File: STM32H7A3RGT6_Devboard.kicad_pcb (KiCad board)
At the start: 2 copper layers, 1 part, among them U1 STM32H7A3RGT6

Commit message: First full draft
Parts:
- added C1: 2u2, Capacitor_SMD:C_0402_1005Metric_Pad0.74x0.62mm_HandSolder, F.Cu at (121.0, 97.2)
- added C10: 1u, Capacitor_SMD:C_0402_1005Metric_Pad0.74x0.62mm_HandSolder, B.Cu at (136.1, 104.5)
- added C11: 1uF, Capacitor_SMD:C_0402_1005Metric_Pad0.74x0.62mm_HandSolder, F.Cu at (106.8, 95.0)
- added C12: 1uF, Capacitor_SMD:C_0402_1005Metric_Pad0.74x0.62mm_HandSolder, F.Cu at (110.7, 96.4)
- added C13: 8pF, Capacitor_SMD:C_0402_1005Metric_Pad0.74x0.62mm_HandSolder, F.Cu at (136.3, 107.5)
- added C14: 8pF, Capacitor_SMD:C_0402_1005Metric_Pad0.74x0.62mm_HandSolder, F.Cu at (140.4, 107.6)
- added C15: 1uF, Capacitor_SMD:C_0603_1608Metric_Pad1.08x0.95mm_HandSolder, F.Cu at (149.3, 100.0)
- added C2: 1u, Capacitor_SMD:C_0402_1005Metric_Pad0.74x0.62mm_HandSolder, F.Cu at (140.3, 95.6)
- added C3: 100n, Capacitor_SMD:C_0402_1005Metric_Pad0.74x0.62mm_HandSolder, F.Cu at (131.2, 107.8)
- added C4: 100n, Capacitor_SMD:C_0402_1005Metric_Pad0.74x0.62mm_HandSolder, F.Cu at (122.2, 98.8)
- added C5: 100n, Capacitor_SMD:C_0402_1005Metric_Pad0.74x0.62mm_HandSolder, F.Cu at (131.2, 92.2)
- added C6: 100n, Capacitor_SMD:C_0402_1005Metric_Pad0.74x0.62mm_HandSolder, F.Cu at (137.5, 97.2)
- added C7: 100n, Capacitor_SMD:C_0402_1005Metric_Pad0.74x0.62mm_HandSolder, F.Cu at (128.8, 107.8)
- added C8: 4u7, Capacitor_SMD:C_0603_1608Metric, F.Cu at (117.8, 97.9)
- added C9: 100n, Capacitor_SMD:C_0402_1005Metric_Pad0.74x0.62mm_HandSolder, F.Cu at (137.8, 103.2)
- added D1: DF2B7AE, Diode_SMD:D_SOD-523, F.Cu at (104.7, 96.9)
- added D2: LED, LED_SMD:LED_0603_1608Metric, F.Cu at (106.9, 107.5)
- added D3: LED, LED_SMD:LED_0603_1608Metric, F.Cu at (103.5, 92.9)
- added J1: USB_C_Receptacle_USB2.0_14P, USBC:USB_C_Receptacle_Molex_217179-0001, F.Cu at (100.0, 100.0)
- added J2: Conn_01x04_Socket, Connector_PinHeader_2.54mm:PinHeader_1x04_P2.54mm_Vertical, F.Cu at (112.0, 100.4)
- added J3: Conn_01x25_PinHeader, Connector_PinHeader_2.54mm:PinHeader_1x25_P2.54mm_Vertical, B.Cu at (98.3, 88.6)
- added J4: Conn_01x25_PinHeader, Connector_PinHeader_2.54mm:PinHeader_1x25_P2.54mm_Vertical, B.Cu at (98.3, 111.4)
- added R1: 5k1, Resistor_SMD:R_0603_1608Metric, F.Cu at (99.9, 93.2)
- added R2: 5k1, Resistor_SMD:R_0603_1608Metric, F.Cu at (99.9, 106.8)
- added R3: 1k, Resistor_SMD:R_0603_1608Metric_Pad0.98x0.95mm_HandSolder, F.Cu at (109.3, 106.8)
- added R4: 5k1, Resistor_SMD:R_0603_1608Metric, F.Cu at (146.8, 99.2)
- added R5: 5k1, Resistor_SMD:R_0603_1608Metric, F.Cu at (103.4, 106.8)
- added R6: 1k, Resistor_SMD:R_0603_1608Metric_Pad0.98x0.95mm_HandSolder, F.Cu at (106.0, 92.1)
- added SW1: RESET, Button_Switch_SMD:SW_Push_1P1T-SH_NO_CK_KMR2xxG, F.Cu at (143.2, 99.2)
- added SW2: BOOT, Button_Switch_SMD:SW_Push_1P1T-SH_NO_CK_KMR2xxG, F.Cu at (106.8, 104.2)
- added U2: AP2127N-3.3TRG1, Package_TO_SOT_SMD:SOT-23, F.Cu at (108.2, 96.8)
- added U3: USBLC6-2SC6, Package_TO_SOT_SMD:SOT-23-6, F.Cu at (106.3, 100.0)
- added Y1: 12MHz, Crystal:Crystal_SMD_2016-4Pin_2.0x1.6mm, F.Cu at (138.4, 107.5)
- moved U1 10.8 mm to (130.0, 100.0), turned to 135 degrees
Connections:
- U1 pad 10: unconnected-(U1-PC2-Pad10) -> /PC2
- U1 pad 11: unconnected-(U1-PC3-Pad11) -> /PC3
- U1 pad 14: unconnected-(U1-PA0-Pad14) -> /PA0
- U1 pad 15: unconnected-(U1-PA1-Pad15) -> /PA1
- U1 pad 16: unconnected-(U1-PA2-Pad16) -> /PA2
- U1 pad 17: unconnected-(U1-PA3-Pad17) -> /PA3
- U1 pad 2: unconnected-(U1-PC13-Pad2) -> /PC13
- U1 pad 20: unconnected-(U1-PA4-Pad20) -> /PA4
- U1 pad 21: unconnected-(U1-PA5-Pad21) -> /PA5
- U1 pad 22: unconnected-(U1-PA6-Pad22) -> /PA6
- U1 pad 23: unconnected-(U1-PA7-Pad23) -> /PA7
- U1 pad 24: unconnected-(U1-PC4-Pad24) -> /PC4
- U1 pad 25: unconnected-(U1-PC5-Pad25) -> /PC5
- U1 pad 26: unconnected-(U1-PB0-Pad26) -> /PB0
- U1 pad 27: unconnected-(U1-PB1-Pad27) -> /PB1
- U1 pad 28: unconnected-(U1-PB2-Pad28) -> /PB2
- U1 pad 29: unconnected-(U1-PB10-Pad29) -> /PB10
- U1 pad 3: unconnected-(U1-PC14-Pad3) -> /PC14
- U1 pad 33: unconnected-(U1-PB12-Pad33) -> /PB12
- U1 pad 34: unconnected-(U1-PB13-Pad34) -> /PB13
- U1 pad 35: unconnected-(U1-PB14-Pad35) -> /PB14
- U1 pad 36: unconnected-(U1-PB15-Pad36) -> /PB15
- U1 pad 37: unconnected-(U1-PC6-Pad37) -> /PC6
- U1 pad 38: unconnected-(U1-PC7-Pad38) -> /PC7
- U1 pad 39: unconnected-(U1-PC9-Pad39) -> /PC9
- U1 pad 4: unconnected-(U1-PC15-Pad4) -> /PC15
- U1 pad 40: unconnected-(U1-PA8-Pad40) -> /PA8
- U1 pad 41: unconnected-(U1-PA9-Pad41) -> /PA9
- U1 pad 42: unconnected-(U1-PA10-Pad42) -> /PA10
- U1 pad 43: unconnected-(U1-PA11-Pad43) -> /USB_D-
- U1 pad 44: unconnected-(U1-PA12-Pad44) -> /USB_D+
- U1 pad 45: unconnected-(U1-PA13-Pad45) -> /SWDIO
- U1 pad 49: unconnected-(U1-PA14-Pad49) -> /SWCLK
- U1 pad 5: unconnected-(U1-PH0-Pad5) -> /OSC_IN
- U1 pad 50: unconnected-(U1-PA15-Pad50) -> /PA15
- U1 pad 51: unconnected-(U1-PC10-Pad51) -> /PC10
- U1 pad 52: unconnected-(U1-PC11-Pad52) -> /PC11
- U1 pad 53: unconnected-(U1-PC12-Pad53) -> /PC12
- U1 pad 54: unconnected-(U1-PD2-Pad54) -> /PD2
- U1 pad 55: unconnected-(U1-PB3-Pad55) -> /PB3
- U1 pad 56: unconnected-(U1-PB4-Pad56) -> /PB4
- U1 pad 57: unconnected-(U1-PB5-Pad57) -> /PB5
- U1 pad 58: unconnected-(U1-PB6-Pad58) -> /PB6
- U1 pad 59: unconnected-(U1-PB7-Pad59) -> /PB7
- U1 pad 6: unconnected-(U1-PH1-Pad6) -> /OSC_OUT
- U1 pad 61: unconnected-(U1-PB8-Pad61) -> /PB8
- U1 pad 62: unconnected-(U1-PB9-Pad62) -> /PB9
- U1 pad 8: unconnected-(U1-PC0-Pad8) -> /PC0
- U1 pad 9: unconnected-(U1-PC1-Pad9) -> /PC1
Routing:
- net +3V3: track 0.00 -> 172.0 mm, vias 0 -> 9
- net VBUS: track 0.00 -> 36.8 mm
- net /BOOT0: track 0.00 -> 25.5 mm, vias 0 -> 2
- net /PA3: track 0.00 -> 24.9 mm
- net /PA4: track 0.00 -> 24.9 mm, vias 0 -> 2
- net /PA2: track 0.00 -> 24.3 mm
- net /PA0: track 0.00 -> 23.0 mm, vias 0 -> 2
- net /PA10: track 0.00 -> 22.8 mm
- net /PC2: track 0.00 -> 22.3 mm, vias 0 -> 2
- net /PA1: track 0.00 -> 22.1 mm
- net /PA15: track 0.00 -> 21.8 mm
- net /PA9: track 0.00 -> 20.5 mm
- net /NRST: track 0.00 -> 20.4 mm, vias 0 -> 2
- net /PA5: track 0.00 -> 20.0 mm
- net /USB_D-: track 0.00 -> 19.8 mm
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- added copper zone on B.Cu, net GND
- added copper zone on F.Cu, net GND
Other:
- board outline added: 63.7 x 25.7 mm

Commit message: update
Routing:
- net GND: track 15.8 -> 22.1 mm, vias 42 -> 59
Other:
- board size 63.7 x 25.7 mm -> 63.8 x 25.7 mm

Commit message: appease DRC checker
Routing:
- net +3V3: track 172.0 -> 170.6 mm
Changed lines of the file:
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@@
 		(tags "Diode SOD523")
 		(property "Reference" "D1"
-			(at 1.9 0 0)
+			(at 1.8 0 0)
 			(layer "F.SilkS")
 			(effects
@@
 		(tags "capacitor handsolder")
 		(property "Reference" "C9"
-			(at -0.022981 -1.154352 0)
+			(at 0.0325 1.25 0)
 			(layer "F.SilkS")
 			(effects
@@
 		(tags "SOT TO_SOT_SMD")
 		(property "Reference" "U2"
-			(at 0 2.25 180)
+			(at 0 2.15 180)
 			(layer "F.SilkS")
 			(effects
@@
 		(tags "capacitor handsolder")
 		(property "Reference" "C11"
-			(at 1.7325 0 0)
+			(at 1.6325 0 0)
 			(layer "F.SilkS")
 			(effects
@@
 		)
 		(property "Value" "BOOT"
-			(at 0 0 0)
+			(at -4.7 0 0)
 			(layer "F.SilkS")
 			(effects
@@
 	)
 	(via
-		(at 110.1 103.9)
+		(at 110.1 103.2)
 		(size 0.7)
 		(drill 0.4)
@@
 		(width 0.5)
 		(layer "B.Cu")
-		(net "+3V3")
-	)
-	(segment
-		(start 137.931371 95.1)
-		(end 138.9 96.068629)
-		(width 0.5)
-		(layer "B.Cu")

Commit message: Fix more DRC check errors
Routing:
- net VBUS: track 36.8 -> 38.2 mm
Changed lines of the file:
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@@
 		(capping no)
 		(filling no)
-		(zone_defaults)
 		(pcbplotparams
 			(layerselection 0x00000000_00000000_55555555_5755f5ff)
@@
 	)
 	(segment
+		(start 106.8 95.6)
+		(end 106.8 96.2375)
+		(width 0.5)
+		(layer "F.Cu")
+		(net "VBUS")
+	)
+	(segment
 		(start 105.3 97.6)
 		(end 106.325 98.625)
@@
 		(width 0.5)
 		(layer "F.Cu")
+		(net "VBUS")
+	)
+	(segment
+		(start 106.8 96.2375)
+		(end 107.3125 96.75)
+		(width 0.5)
+		(layer "F.Cu")

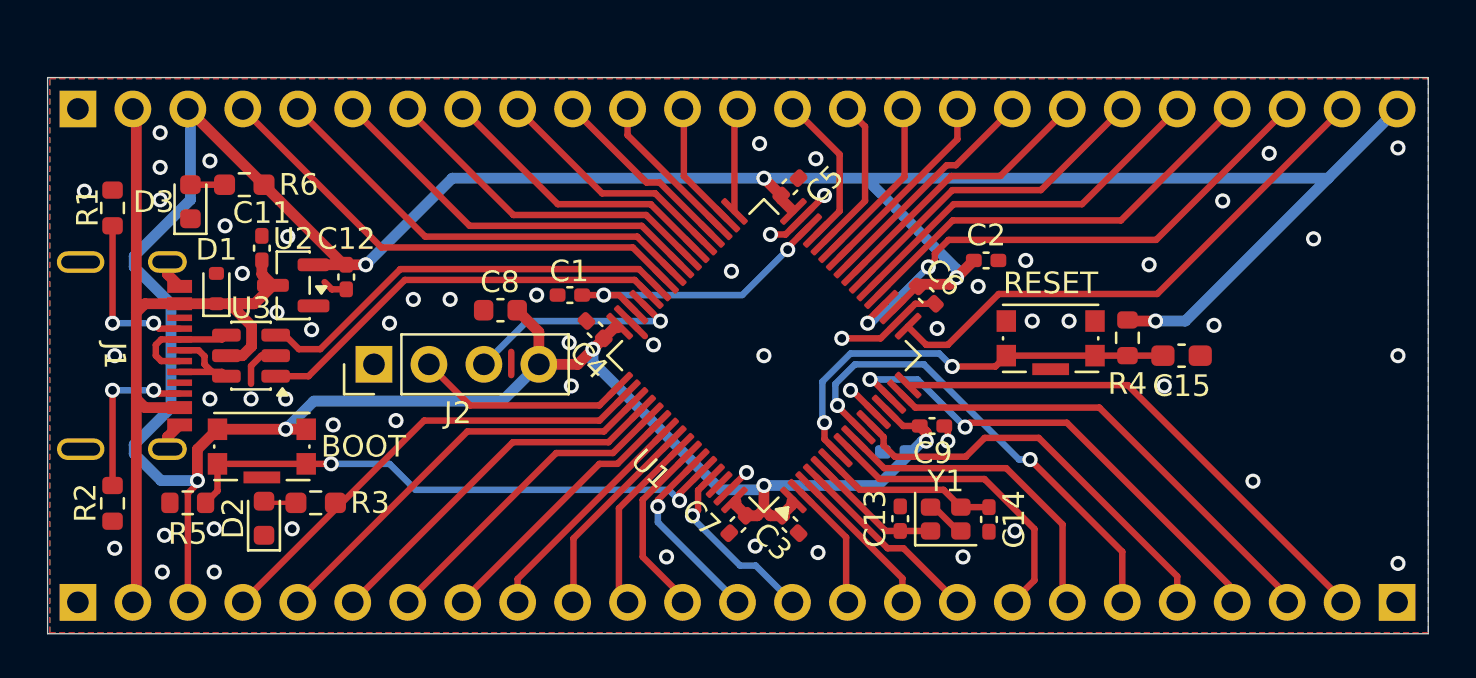
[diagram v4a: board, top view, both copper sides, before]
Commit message: Silkscreen and more vias
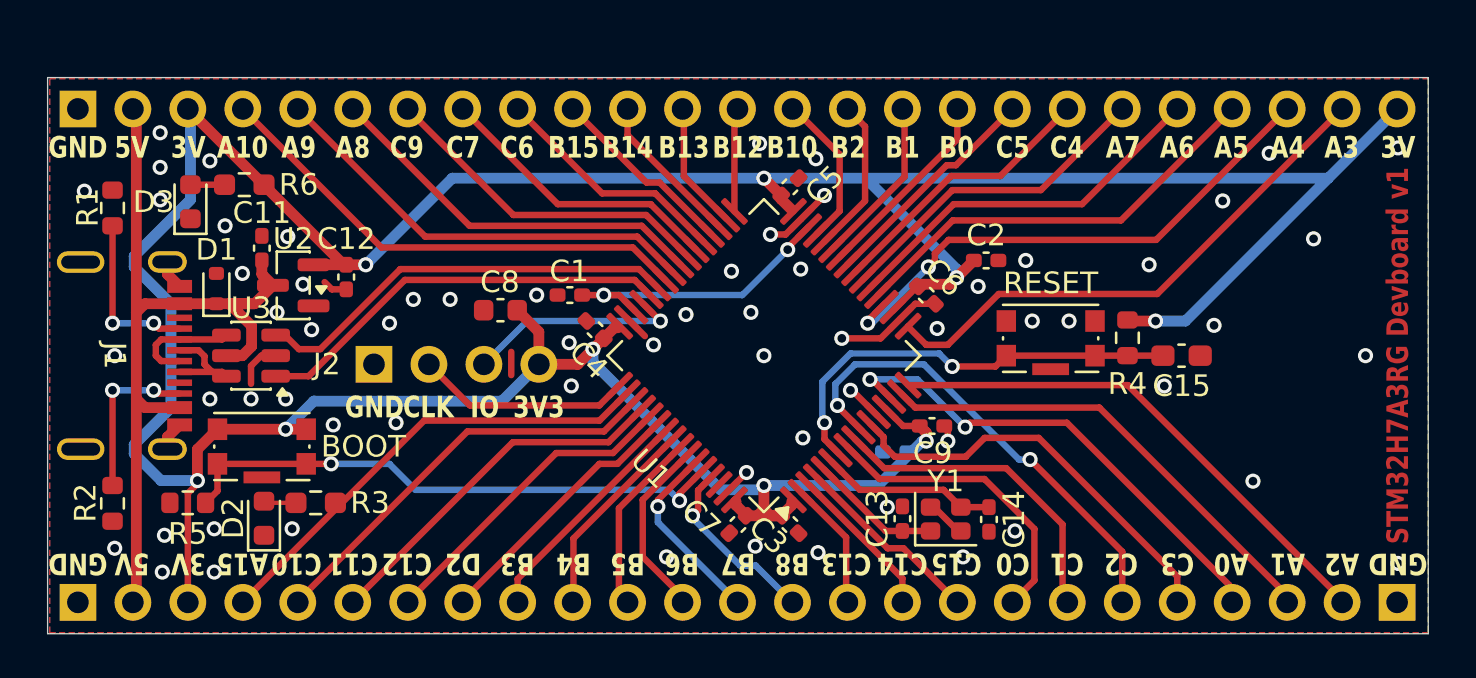
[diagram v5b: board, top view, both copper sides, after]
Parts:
- moved C13 0.10 mm to (136.4, 107.5)
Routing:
- net +3V3: track 170.6 -> 171.7 mm
- net GND: vias 59 -> 65
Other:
- board text added: "3V"
- board text added: "3V3"
- board text added: "5V"
- board text added: "A0"
- board text added: "A1"
- board text added: "A10"
- board text added: "A15"
- board text added: "A2"
- board text added: "A3"
- board text added: "A4"
- board text added: "A5"
- board text added: "A6"
- board text added: "A7"
- board text added: "A8"
- board text added: "A9"
- board text added: "B0"
- board text added: "B1"
- board text added: "B10"
- board text added: "B12"
- board text added: "B13"
- board text added: "B14"
- board text added: "B15"
- board text added: "B2"
- board text added: "B3"
- board text added: "B4"
- board text added: "B5"
- board text added: "B6"
- board text added: "B7"
- board text added: "B8"
- board text added: "C0"
- board text added: "C1"
- board text added: "C10"
- board text added: "C11"
- board text added: "C12"
- board text added: "C13"
- board text added: "C14"
- board text added: "C15"
- board text added: "C2"
- board text added: "C3"
- board text added: "C4"
- board text added: "C5"
- board text added: "C6"
- board text added: "C7"
- board text added: "C9"
- board text added: "CLK"
- board text added: "D2"
- board text added: "GND"
- board text added: "IO"
- board text added: "STM32H7A3RG Devboard v1"

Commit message: QSPI DRAM support
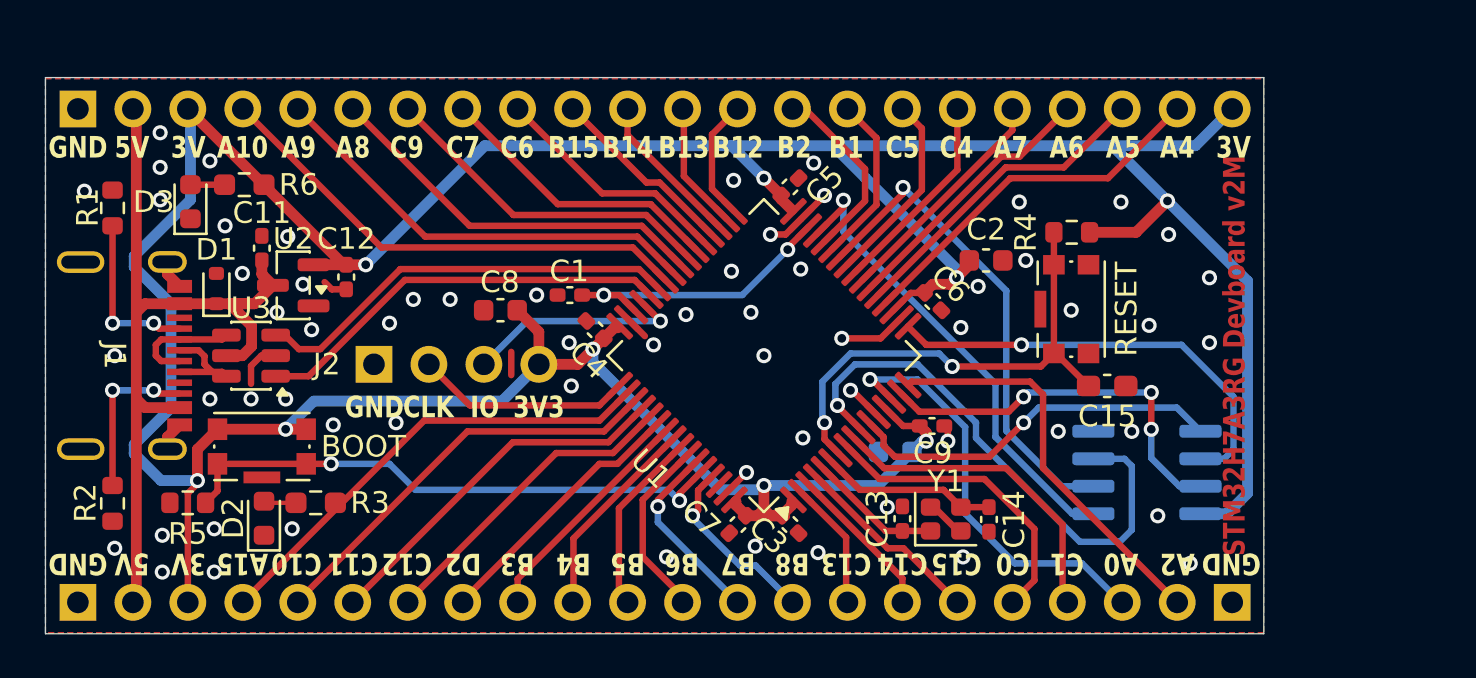
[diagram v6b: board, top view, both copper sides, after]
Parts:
- added U4: APS6404L-3SQR-SN, Package_SO:SOIC-8_3.9x4.9mm_P1.27mm, B.Cu at (147.7, 105.4)
- C10, C2: footprint Capacitor_SMD:C_0402_1005Metric_Pad0.74x0.62mm_HandSolder -> Capacitor_SMD:C_0603_1608Metric
- J3, J4: value Conn_01x25_PinHeader -> Conn_01x22_Socket; footprint Connector_PinHeader_2.54mm:PinHeader_1x25_P2.54mm_Vertical -> Connector_PinHeader_2.54mm:PinHeader_1x22_P2.54mm_Vertical
- moved R4 5.51 mm to (144.2, 94.3), turned to 180 degrees
- moved C15 3.71 mm to (145.9, 101.4)
- moved SW1 1.65 mm to (144.2, 97.8), turned to 90 degrees
- moved C6 0.42 mm to (137.8, 97.5)
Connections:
- J3 pad 14: /PB10 -> /PB2
- J3 pad 15: /PB2 -> /PB1
- J3 pad 16: /PB1 -> /PC5
- J3 pad 17: /PB0 -> /PC4
- J3 pad 18: /PC5 -> /PA7
- J3 pad 19: /PC4 -> /PA6
- J3 pad 20: /PA7 -> /PA5
- J3 pad 21: /PA6 -> /PA4
- J3 pad 22: /PA5 -> +3V3
- J4 pad 20: /PC2 -> /PA0
- J4 pad 21: /PC3 -> /PA2
- J4 pad 22: /PA0 -> GND
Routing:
- net /PB10: track 7.19 -> 21.9 mm, vias 0 -> 1
- net /PB0: track 9.12 -> 22.8 mm, vias 0 -> 1
- net +3V3: track 171.7 -> 181.8 mm
- net /PA4: track 24.9 -> 17.2 mm, vias 2 -> 0
- net /PA2: track 24.3 -> 18.7 mm
- net /PA5: track 20.0 -> 14.9 mm
- net /PA6: track 17.6 -> 12.6 mm
- net /PA7: track 15.3 -> 10.8 mm
- net /PA3: track 24.9 -> 20.5 mm, vias 0 -> 1
- net /PA1: track 22.1 -> 18.2 mm, vias 0 -> 3
- net /PC4: track 13.0 -> 9.53 mm
- net /PC2: track 22.3 -> 25.7 mm, vias 2 -> 1
- net /PA0: track 23.0 -> 19.7 mm, vias 2 -> 1
- net /NRST: track 20.4 -> 23.2 mm
- net GND: track 22.1 -> 20.2 mm, vias 65 -> 63
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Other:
- board size 63.8 x 25.7 mm -> 56.3 x 25.7 mm
- board text added: "STM32H7A3RG Devboard v2M"
- board text removed: "A1"
- board text removed: "A3"
- board text removed: "B0"
- board text removed: "B10"
- board text removed: "C2"
- board text removed: "C3"
- board text removed: "STM32H7A3RG Devboard v1"
